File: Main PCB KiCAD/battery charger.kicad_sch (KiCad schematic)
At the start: 5 parts, among them J10 Battery, U5 BQ24075RGT, U6 BQ27441-G1

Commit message: battery charging
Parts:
- removed J10: Battery, Connector_Molex:Molex_Nano-Fit_105309-xx02_1x02_P2.50mm_Vertical, symbol Connector_Generic:Conn_01x02
- removed U5: BQ24075RGT, Package_DFN_QFN:VQFN-16-1EP_3x3mm_P0.5mm_EP1.6x1.6mm, symbol Battery_Management:BQ24075RGT
- removed U6: BQ27441-G1, Package_SON:Texas_S-PDSO-N12, symbol Battery_Management:BQ27441-G1
- added BT1, BT2, BT3: 18650, symbol Device:Battery_Cell
- added C10: 100nF, Capacitor_SMD:C_0805_2012Metric_Pad1.18x1.45mm_HandSolder, symbol Device:C_Small
- added C6, C8, C9: 1u, Capacitor_SMD:C_0805_2012Metric_Pad1.18x1.45mm_HandSolder, symbol Device:C_Small
- added C7: 1uF, Capacitor_SMD:C_0805_2012Metric_Pad1.18x1.45mm_HandSolder, symbol Device:C_Small
- added D12: 1N5819HW-FDICT, Diode_SMD:D_SOD-123, symbol Device:D_Schottky_Small_Filled
- added D13, D14, D15: LED, LED_SMD:LED_0805_2012Metric_Pad1.15x1.40mm_HandSolder, symbol Device:LED_Small_Filled
- added J10: USB_B_Micro, Connector_USB:USB_Micro-B_Amphenol_10103594-0001LF_Horizontal, symbol Connector:USB_B_Micro
- added JP4: LEDs, Jumper:SolderJumper-2_P1.3mm_Bridged_RoundedPad1.0x1.5mm, symbol Jumper:SolderJumper_2_Bridged
- added Q1, Q2: Q_NMOS_DSG, Package_TO_SOT_SMD:SOT-23, symbol Device:Q_NMOS_DSG
- added R11: 1k, Resistor_SMD:R_0805_2012Metric_Pad1.20x1.40mm_HandSolder, symbol Device:R_Small
- added R12, R13, R14, R16: 330, Resistor_SMD:R_0805_2012Metric_Pad1.20x1.40mm_HandSolder, symbol Device:R_Small
- added R15, R17, R18: 22k, Resistor_SMD:R_0805_2012Metric_Pad1.20x1.40mm_HandSolder, symbol Device:R_Small
- added R19: 2.7k, Resistor_SMD:R_0805_2012Metric_Pad1.20x1.40mm_HandSolder, symbol Device:R_Small
- added TH1: Thermistor_NTC, Resistor_SMD:R_0805_2012Metric_Pad1.15x1.40mm_HandSolder, symbol Device:Thermistor_NTC
- added U5: AP7215-33YG-13, BatteryModule:AP7215-33YG-13, symbol 2019-08-09_22-35-48:AP7215-33YG-13
- added U6: MCP73834T-FCI/UN, digikey-footprints:MSOP-10_W3mm, symbol dk_PMIC-Battery-Chargers:MCP73833-AMI_UN
- added U7: AP9101CAK6-ANTRG1, BatteryModule:SOT95P280X140-6N, symbol AP9101CAK6-ANTRG1:AP9101CAK6-ANTRG1
- R5, R6: value 1k -> 10k
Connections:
- net +Batt: now also BT1.1 (+), BT2.1 (+), BT3.1 (+), C7.1, C8.1, R16.1, U5.2 (VIN), U6.10 (VBAT), U6.9 (VBAT)
- net -Batt: now also BT1.2 (-), BT2.2 (-), BT3.2 (-), C10.2, C7.2, Q1.2 (S), U7.6 (VSS)
- new net: R11.1, U6.6 (PROG)
- new net: TH1.1, U6.8 (THERM)
- new net: D12.2 (A), J10.1 (VBUS)
- new net: D13.1 (K), R12.1
- new net: D13.2 (A), D14.2 (A), D15.2 (A), JP4.1 (A)
- new net: D14.1 (K), R13.1
- new net: D15.1 (K), R14.1
- new net: C10.1, R16.2, U7.5 (VDD)
- new net: R19.1, U7.2 (VM)
- new net: Q1.1 (D), Q2.1 (D)
- new net: Q1.3 (G), U7.1 (DO)
- new net: Q2.3 (G), U7.3 (CO)
- new net +3.3V: C9.1, R15.1, R17.1, R18.1, U5.3 (VROUT)
- new net +Solar: C6.1, D12.1 (K), JP4.2 (B), U6.1 (VDD), U6.2 (VDD)
- new net GND: C6.2, C8.2, C9.2, J10.5 (GND), Q2.2 (S), R11.2, R19.2, TH1.2, U5.1 (GND), U6.5 (VSS)
- new net PG: R14.2, R18.2, U6.7 (~{PG}(~{TE}))
- new net Status1: R12.2, R15.2, U6.3 (STAT1)
- new net Status2: R13.2, R17.2, U6.4 (STAT2)
- no-connect marks 0 -> 4
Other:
- note removed: "https://thepihut.com/products/sparkfun-battery-babysitter-lipo-battery-manager https://cdn.sparkfun.com/assets/learn_tutorials/5/3/0/sparkfun-battery-babysitter-v10-schematic.pdf"

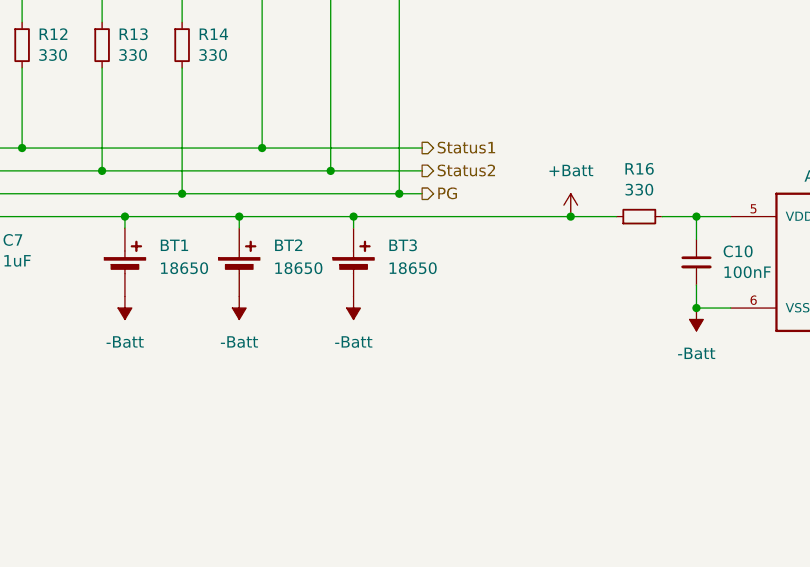
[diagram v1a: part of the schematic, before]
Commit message: updated 18650
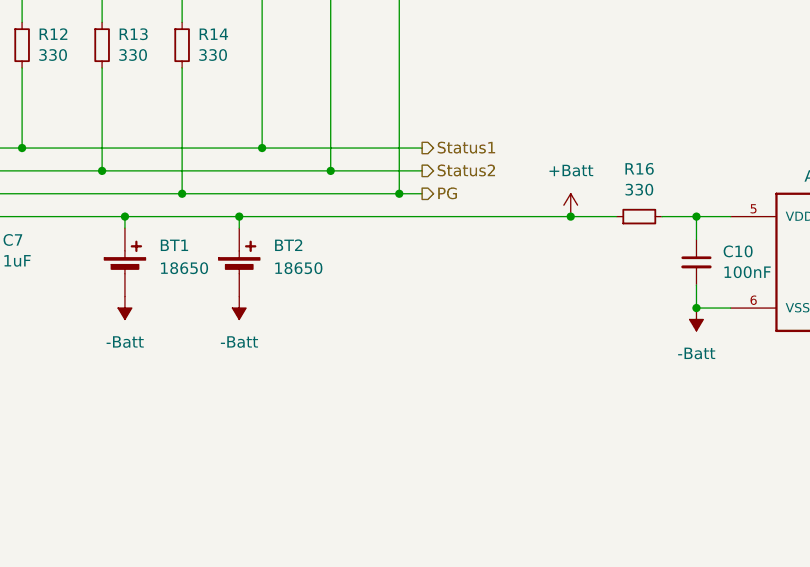
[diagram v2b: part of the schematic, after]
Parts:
- removed BT3: 18650, symbol Device:Battery_Cell
- BT1, BT2: footprint (none) -> Batteries:18650 Holder
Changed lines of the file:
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@@
 	)
 	(junction
-		(at 181.61 102.87)
-		(diameter 0)
-		(color 0 0 0 0)
-	)
-	(junction
 		(at 26.67 41.91)
 		(diameter 0)
@@
 	(wire
 		(pts
-			(xy 181.61 102.87) (xy 205.74 102.87)
-		)
-		(stroke
-			(width 0)
-			(type default)
-		)
-	)
-	(wire
-		(pts
 			(xy 153.67 69.85) (xy 162.56 69.85)
 		)
@@
 	(wire
 		(pts
-			(xy 168.91 102.87) (xy 181.61 102.87)
+			(xy 168.91 102.87) (xy 205.74 102.87)
 		)
 		(stroke
@@
 	(wire
 		(pts
-			(xy 181.61 102.87) (xy 181.61 104.14)
-		)
-		(stroke
-			(width 0)
-			(type default)
-		)
-	)
-	(wire
-		(pts
 			(xy 189.23 97.79) (xy 179.07 97.79)
 		)
@@
 			)
 		)
-		(property "Footprint" ""
+		(property "Footprint" "Batteries:18650 Holder"
 			(at 156.21 107.696 90)
 			(effects
@@
 	(symbol
 		(lib_id "power:-BATT")
-		(at 181.61 111.76 180)
-		(unit 1)
-		(exclude_from_sim no)
-		(in_bom yes)
-		(on_board yes)
-		(dnp no)
-		(fields_autoplaced yes)
-		(property "Reference" "#PWR010"
-			(at 181.61 107.95 0)
-			(effects
-				(font
-					(size 1.27 1.27)
-				)
-				(hide yes)
-			)
-		)
-		(property "Value" "-Batt"
-			(at 181.61 116.84 0)
-			(effects
-				(font
-					(size 1.27 1.27)
-				)
-			)
-		)
-		(property "Footprint" ""
-			(at 181.61 111.76 0)
-			(effects
-				(font
-					(size 1.27 1.27)
-				)
-				(hide yes)
-			)
-		)
-		(property "Datasheet" ""
-			(at 181.61 111.76 0)
-			(effects
-				(font
-					(size 1.27 1.27)
-				)
-				(hide yes)
-			)
-		)
-		(property "Description" "Power symbol creates a global label with name \"-Batt\""
-			(at 181.61 111.76 0)
-			(effects
-				(font
-					(size 1.27 1.27)
-				)
-				(hide yes)
-			)
-		)
-		(pin "1"
-		)
-		(instances
-			(project "Buoy PCB"
-				(path "/a041e2a6-7d41-458c-91f3-753821d3dfe9/435dc0a6-dd3d-415b-8797-8ccd529132c2"
-					(reference "#PWR010")
-					(unit 1)
-				)
-			)
-		)
-	)
-	(symbol
-		(lib_id "power:-BATT")
 		(at 242.57 130.81 180)
 		(unit 1)
@@
 	)
 	(symbol
-		(lib_id "Device:Battery_Cell")
-		(at 181.61 109.22 0)
-		(unit 1)
-		(exclude_from_sim no)
-		(in_bom yes)
-		(on_board yes)
-		(dnp no)
-		(fields_autoplaced yes)
-		(property "Reference" "BT3"
-			(at 185.42 106.1084 0)
-			(effects
-				(font
-					(size 1.27 1.27)
-				)
-				(justify left)
-			)
-		)
-		(property "Value" "18650"
-			(at 185.42 108.6484 0)
-			(effects
-				(font
-					(size 1.27 1.27)
-				)
-				(justify left)
-			)
-		)
-		(property "Footprint" ""
-			(at 181.61 107.696 90)
-			(effects
-				(font
-					(size 1.27 1.27)
-				)
-				(hide yes)
-			)
-		)
-		(property "Datasheet" "~"
-			(at 181.61 107.696 90)
-			(effects
-				(font
-					(size 1.27 1.27)
-				)
-				(hide yes)
-			)
-		)
-		(property "Description" "Single-cell battery"
-			(at 181.61 109.22 0)
-			(effects
-				(font
-					(size 1.27 1.27)
-				)
-				(hide yes)
-			)
-		)
-		(pin "1"
-		)
-		(pin "2"
-		)
-		(instances
-			(project "Buoy PCB"
-				(path "/a041e2a6-7d41-458c-91f3-753821d3dfe9/435dc0a6-dd3d-415b-8797-8ccd529132c2"
-					(reference "BT3")
-					(unit 1)
-				)
-			)
-		)
-	)
-	(symbol
 		(lib_id "Device:R_Small")
 		(at 26.67 36.83 0)
@@
 			)
 		)
-		(property "Footprint" ""
+		(property "Footprint" "Batteries:18650 Holder"
 			(at 168.91 107.696 90)
 			(effects

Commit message: clean
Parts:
- BT1, BT2: footprint Batteries:18650 Holder -> Battery:BatteryHolder_Keystone_1042_1x18650
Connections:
- net +Solar: no longer C6.1, JP4.2 (B), U6.1 (VDD), U6.2 (VDD)
- net GND: no longer C6.2, Q2.2 (S), R19.2
- net +3.3V renamed +3.3V_bat
- new net +Solar_Batt: C6.1, JP4.2 (B), U6.1 (VDD), U6.2 (VDD)
- new net GND_Batt: C6.2, Q2.2 (S), R19.2
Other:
- moved on the sheet: C9

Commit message: update
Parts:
- D13, D14, D15: value LED -> RED
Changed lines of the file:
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@@
 			)
 		)
-		(property "Value" "LED"
+		(property "Value" "RED"
 			(at 147.7518 74.9808 90)
 			(effects
@@
 			)
 		)
-		(property "Value" "LED"
+		(property "Value" "RED"
 			(at 156.6418 74.9808 90)
 			(effects
@@
 			)
 		)
-		(property "Value" "LED"
+		(property "Value" "RED"
 			(at 165.5318 74.9808 90)
 			(effects

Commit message: update
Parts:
- removed BT1, BT2: 18650, Battery:BatteryHolder_Keystone_1042_1x18650, symbol Device:Battery_Cell
- added J11: Battery 1, Connector_JST:JST_PH_S2B-PH-K_1x02_P2.00mm_Horizontal, symbol Connector_Generic:Conn_01x02
- added J12: Battery 2, Connector_JST:JST_PH_S2B-PH-K_1x02_P2.00mm_Horizontal, symbol Connector_Generic:Conn_01x02
- renumbered C7 to C10, C10 to C11, C6 to C7, D12 to D10, D13 to D11, D14 to D12, D15 to D13, JP4 to JP3, R5 to R11, R6 to R12, R11 to R13, R12 to R14, R13 to R15, R14 to R16, R15 to R17, R17 to R18, R18 to R19, R16 to R20, R19 to R21, U5 to U3, U6 to U4, U7 to U5
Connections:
- net +Batt: now also J11.1 (Pin_1), J12.1 (Pin_1)
- net -Batt: now also J11.2 (Pin_2), J12.2 (Pin_2)
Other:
- note added: "https://shop.pimoroni.com/products/lipo-battery-pack?variant=20429082247"

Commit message: cleanup
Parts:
- removed D10: 1N5819HW-FDICT, Diode_SMD:D_SOD-123, symbol Device:D_Schottky_Small_Filled
- removed J10: USB_B_Micro, Connector_USB:USB_Micro-B_Amphenol_10103594-0001LF_Horizontal, symbol Connector:USB_B_Micro
- added C1, C3: 1u, Capacitor_SMD:C_0805_2012Metric_Pad1.18x1.45mm_HandSolder, symbol Device:C_Small
- U4: footprint digikey-footprints:MSOP-10_W3mm -> Silicon-Standard:MSOP-10-GNDPAD
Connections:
- net +Solar_Batt: now also C3.1
- net -Batt: now also C1.2
- net GND_Batt: now also C3.2
- net PG: now also D13.1 (K); no longer R16.2
- net Status1: now also D11.1 (K); no longer R14.2
- net Status2: now also D12.1 (K); no longer R15.2
- net V_Batt_An: now also C1.1
- net at R14.1: now also JP3.1 (A), R15.1, R16.1; no longer D11.1 (K)
- new net: D11.2 (A), R14.2
- new net: D12.2 (A), R15.2
- new net: D13.2 (A), R16.2
- no-connect marks 4 -> 0
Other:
- moved on the sheet: D11, D12, D13, R14, R15, R16, TH1
